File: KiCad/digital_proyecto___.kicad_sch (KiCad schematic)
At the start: 38 parts, among them J2 DE9_Pins, J3 DE9_Pins, U1 MCP2551-I-SN, U2 LM393, U3 A1101xLH, U4 LM393, U6 MAX3232, U7 A1101xLH

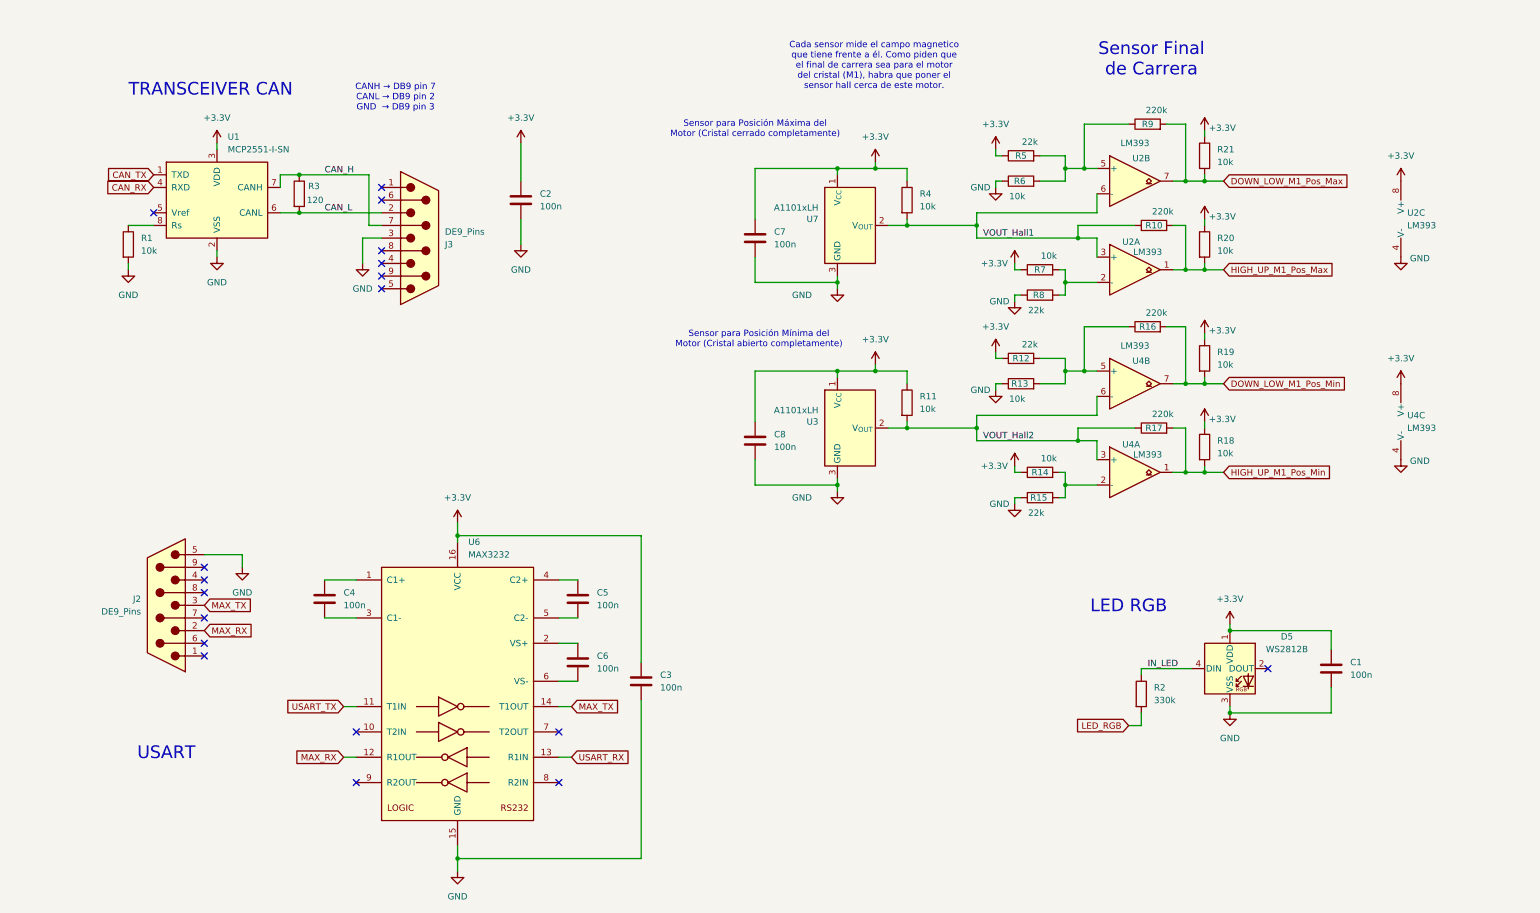
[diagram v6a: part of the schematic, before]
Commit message: Esquematico acabado y readme estructura base y componentes acabado y puesto el DB.
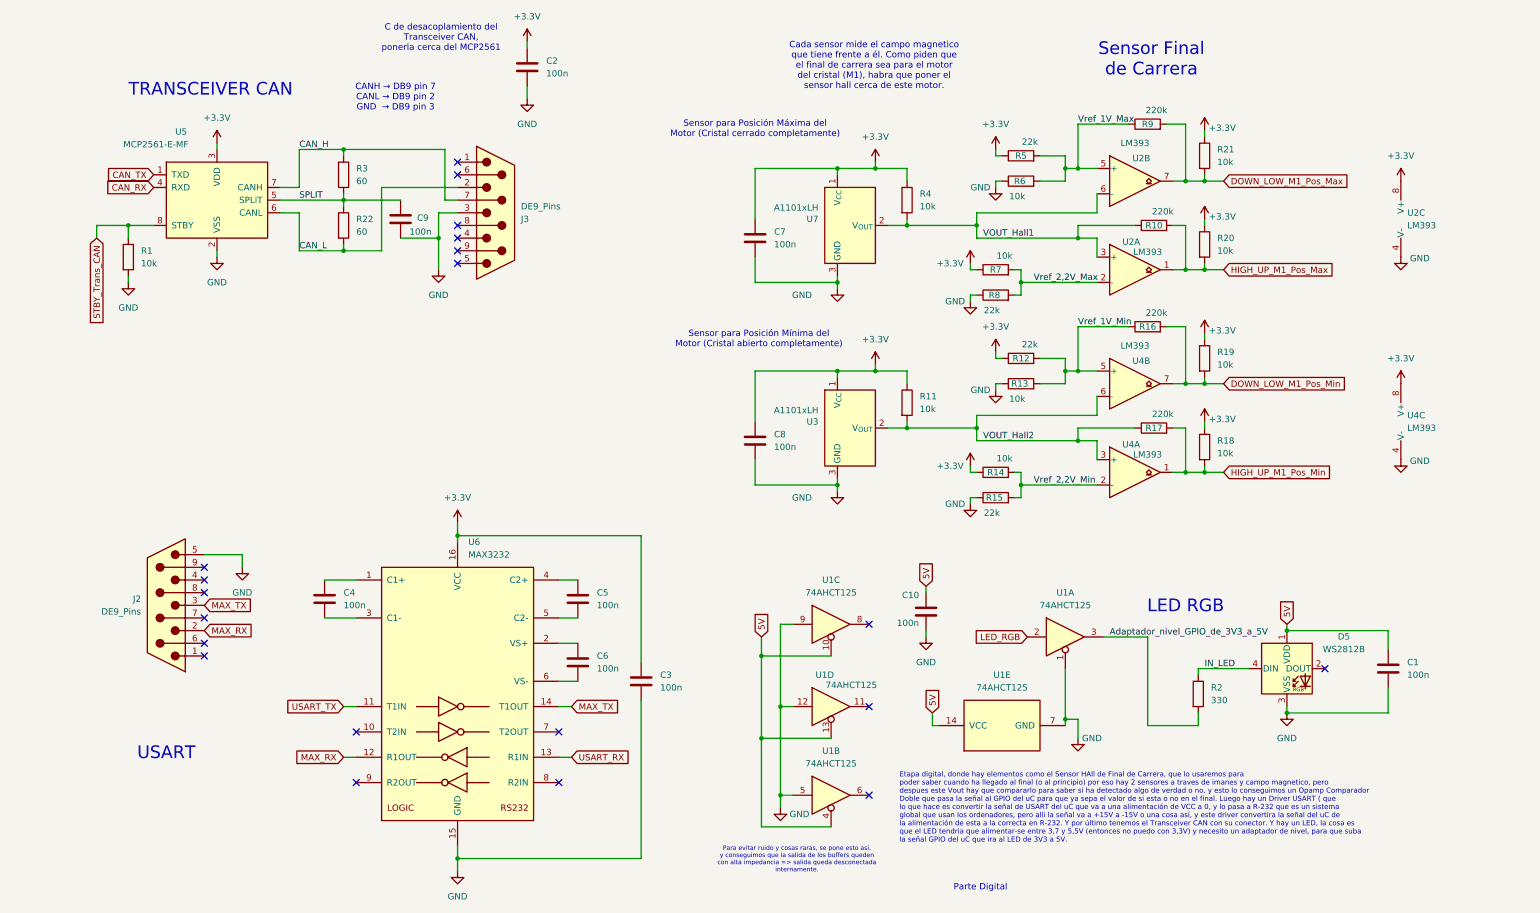
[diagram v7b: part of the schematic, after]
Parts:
- removed U1: MCP2551-I-SN, Package_SO:SOIC-8_3.9x4.9mm_P1.27mm, symbol Interface_CAN_LIN:MCP2551-I-SN
- added C10, C9: 100n, Capacitor_SMD:C_0805_2012Metric, symbol Device:C
- added R22: 60, Resistor_SMD:R_0805_2012Metric, symbol Device:R
- added U1: 74AHCT125, Package_SO:SOIC-14_3.9x8.7mm_P1.27mm, symbol 74xx:74AHCT125
- added U5: MCP2561-E-MF, Package_SO:SOIC-8-1EP_3.9x4.9mm_P1.27mm_EP2.29x3mm, symbol Interface_CAN_LIN:MCP2561-E-MF
- R2: value 330k -> 330
- R3: value 120 -> 60
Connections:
- net +3.3V: now also U5.3 (VDD); no longer C1.1, D5.1 (VDD)
- net CAN_H: now also U5.7 (CANH)
- net CAN_L: now also R22.2, U5.6 (CANL); no longer R3.2
- net CAN_RX: now also U5.4 (RXD)
- net CAN_TX: now also U5.1 (TXD)
- net GND: now also C10.2, C9.2, U1.1, U1.12, U1.5, U1.7 (GND), U1.9, U5.2 (VSS), U5.9 (VSS)
- net LED_RGB: now also U1.2; no longer R2.2
- net Vref_2,2V_Max: now reaches R7.2, R8.2, U2.2 (-)
- net Vref_1V_Min: now reaches R12.2, R13.2, R16.1, U4.5 (+)
- net Vref_1V_Max: now reaches R5.2, R6.2, R9.1, U2.5 (+)
- net STBY_Trans_CAN: now reaches R1.1
- net STBY_Trans_CAN: now also U5.8 (STBY)
- net Vref_2,2V_Min: now reaches R14.2, R15.2, U4.2 (-)
- new net 5V: C1.1, C10.1, D5.1 (VDD), U1.10, U1.13, U1.14 (VCC), U1.4
- new net Adaptador_nivel_GPIO_de_3V3_a_5V: R2.2, U1.3
- new net SPLIT: C9.1, R22.1, R3.2, U5.5 (SPLIT)
- no-connect marks 19 -> 21
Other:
- note added: "C de desacoplamiento del Transceiver CAN, ponerla cerca del MCP2561"
- note added: "Etapa digital, donde hay elementos como el Sensor HAll de Final de Carrera, que lo usaremos para poder saber cuando ha llegado al final (o al principio) por eso hay 2 sensores a traves de imanes y campo magnetico, pero despues este Vout hay que compararlo para saber si ha detectado algo de verdad o no, y esto lo conseguimos un Opamp Comparador Doble que pasa la señal al GPIO del uC para que ya se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"
- note added: "Para evitar ruido y cosas raras, se pone esto así, y conseguimos que la salida de los buffers queden con alta impedancia => salida queda desconectada internamente."
- note added: "Parte Digital"
- moved on the sheet: C1, C2, D5, J3, R1, R14, R15, R2, R7, R8

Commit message: Cambios al esquematico por SEsión 3
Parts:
- removed U1: 74AHCT125, Package_SO:SOIC-14_3.9x8.7mm_P1.27mm, symbol 74xx:74AHCT125
- removed U4: LM393, Package_SO:SOIC-8_5.3x6.2mm_P1.27mm, symbol Comparator:LM393
- added C33, C34: 100n, Capacitor_SMD:C_0805_2012Metric, symbol Device:C
- added U1: 74AHCT1G125, symbol 74xGxx:74AHCT1G125
- added U3: LM393, symbol Comparator:LM393
- U2: footprint Package_SO:SOIC-8_5.3x6.2mm_P1.27mm -> (none)
- renumbered C4 to C23, C9 to C24, C2 to C25, C5 to C26, C6 to C27, C3 to C28, C7 to C29, C8 to C30, C10 to C31, C1 to C32, J2 to J10, J3 to J11, R1 to R21, R3 to R22, R22 to R23, R4 to R24, R11 to R25, R7 to R26, R8 to R27, R14 to R28, R15 to R29, R5 to R30, R6 to R31, R12 to R32, R13 to R33, R9 to R34, R16 to R35, R10 to R36, R17 to R37, R2 to R38, R21 to R39, R20 to R40, R19 to R41, R18 to R42, U5 to U10, U6 to U11, U7 to U12, U3 to U13
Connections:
- net Adaptador_nivel_GPIO_de_3V3_a_5V is gone; now on net IN_LED: R38.2
- net +3.3V: now also C33.1, C34.1, U3.8 (V+)
- net 5V: now also U1.5 (VCC)
- net DOWN_LOW_M1_Pos_Max: now also U2.1; no longer U2.7
- net DOWN_LOW_M1_Pos_Min: now also U3.1
- net GND: now also C33.2, C34.2, U1.1, U1.3 (GND), U3.4 (V-)
- net HIGH_UP_M1_Pos_Max: now also U2.7; no longer U2.1
- net HIGH_UP_M1_Pos_Min: now also U3.7
- net IN_LED: no longer R38.1
- net LED_RGB: now also U1.2
- net VOUT_Hall1: now also U2.2 (-), U2.5 (+); no longer U2.3 (+), U2.6 (-)
- net VOUT_Hall2: now also U3.2 (-), U3.5 (+)
- net Vref_1V_Max: now also U2.3 (+); no longer U2.5 (+)
- net Vref_1V_Min: now also U3.3 (+)
- net Vref_2,2V_Max: now also U2.6 (-); no longer U2.2 (-)
- net Vref_2,2V_Min: now also U3.6 (-)
- new net GPIO_3V3_a_5V: R38.1, U1.4
- no-connect marks 21 -> 18
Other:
- note removed: "Para evitar ruido y cosas raras, se pone esto así, y conseguimos que la salida de los buffers queden con alta impedancia => salida queda desconectada internamente."
- moved on the sheet: C31, R38
